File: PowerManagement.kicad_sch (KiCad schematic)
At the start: 27 parts, among them Q1 NMOS, U2 OKI-78SR-3.3_1.5-W36-C, U3 LM34966

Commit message: schematics done
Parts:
- removed C1: 100p, Capacitor_SMD:C_0603_1608Metric_Pad1.08x0.95mm_HandSolder, symbol Device:C
- removed C3: 10n, Capacitor_SMD:C_0603_1608Metric_Pad1.08x0.95mm_HandSolder, symbol Device:C
- removed C4, C6: 22n, Capacitor_SMD:C_0603_1608Metric_Pad1.08x0.95mm_HandSolder, symbol Device:C
- removed C5: 220p, Capacitor_SMD:C_0603_1608Metric_Pad1.08x0.95mm_HandSolder, symbol Device:C
- removed D1, D2: D, symbol Device:D
- removed L1: L, symbol Device:L
- removed Q1: NMOS, Package_TO_SOT_SMD:SOT-223-3_TabPin2, symbol Simulation_SPICE:NMOS
- removed R1, R2, R3: R, symbol Device:R
- removed R10: 11k3, Capacitor_SMD:C_0603_1608Metric_Pad1.08x0.95mm_HandSolder, symbol Device:R
- removed R11: 0, Resistor_SMD:R_0603_1608Metric_Pad0.98x0.95mm_HandSolder, symbol Device:R
- removed R12, R4: 10m, Resistor_SMD:R_0603_1608Metric_Pad0.98x0.95mm_HandSolder, symbol Device:R
- removed R5: 100, Resistor_SMD:R_0603_1608Metric_Pad0.98x0.95mm_HandSolder, symbol Device:R
- removed R7: 10k, Resistor_SMD:R_0603_1608Metric_Pad0.98x0.95mm_HandSolder, symbol Device:R
- removed R8: 6k8, Resistor_SMD:R_0603_1608Metric_Pad0.98x0.95mm_HandSolder, symbol Device:R
- removed R9: 49k9, Resistor_SMD:R_0603_1608Metric_Pad0.98x0.95mm_HandSolder, symbol Device:R
- removed U2: OKI-78SR-3.3_1.5-W36-C, Converter_DCDC:Converter_DCDC_Murata_OKI-78SR_Vertical, symbol Converter_DCDC:OKI-78SR-3.3_1.5-W36-C
- removed U3: LM34966, Package_SO:HTSSOP-14-1EP_4.4x5mm_P0.65mm_EP3.4x5mm_Mask3x3.1mm_ThermalVias, symbol 10_ICs:LM34966
- added C30, C33: 10n, Capacitor_SMD:C_0603_1608Metric_Pad1.08x0.95mm_HandSolder, symbol Device:C
- added C31, C32, C53: 1u, Capacitor_SMD:C_0805_2012Metric_Pad1.18x1.45mm_HandSolder, symbol Device:C
- added C54: 100n, Capacitor_SMD:C_0603_1608Metric_Pad1.08x0.95mm_HandSolder, symbol Device:C
- added C55: 1n, Capacitor_SMD:C_0603_1608Metric_Pad1.08x0.95mm_HandSolder, symbol Device:C
- added F1, F2, F3, F4: Polyfuse_Small, symbol Device:Polyfuse_Small
- added U12: OKI-78SR-3.3_1.5-W36H-C, Converter_DCDC:Converter_DCDC_Murata_OKI-78SR_Horizontal, symbol Converter_DCDC:OKI-78SR-3.3_1.5-W36H-C
- added U13: OKI-78SR-12_1.0-W36H-C, Converter_DCDC:Converter_DCDC_Murata_OKI-78SR_Horizontal, symbol Converter_DCDC:OKI-78SR-12_1.0-W36H-C
- added U14: MCP1501-30xSN, Package_SO:SOIC-8_3.9x4.9mm_P1.27mm, symbol Reference_Voltage:MCP1501-30xSN
- C2: value 1u -> 100n; footprint Capacitor_SMD:C_0805_2012Metric_Pad1.18x1.45mm_HandSolder -> Capacitor_SMD:C_0603_1608Metric_Pad1.08x0.95mm_HandSolder
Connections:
- net VCC is gone; now on net GND: C2.2
- net GND: now also C30.2, C31.1, C32.1, C33.2, C53.1, C54.2, C55.2, U12.2 (GND), U13.2 (GND), U14.2 (GND), U14.4 (GND), U14.5 (GND), U14.6 (GND); no longer C2.1
- net P3V3: now also C2.1, F3.2, U14.1 (VDD), U14.3 (~{SHDN}); no longer C26.2, C27.1
- net P24_6S_UNREGULATED renamed P15V-20V_5S_FUSED
- net P15V-20V_5S_FUSED: now also C30.1, C31.2, F2.2, U12.1 (IN), U13.1 (IN)
- new net: C26.2, C27.1, F3.1, U12.3 (OUT)
- new net: C32.2, C33.1, F4.1, U13.3 (OUT)
- new net P12V: F4.2
- new net P15V-20V_5S_UNREGULATED: F2.1
- new net P3V_REF: C53.2, C54.1, C55.1, U14.7 (OUT), U14.8 (FB)
- new net PHV: F1.2
- new net step-up/PHV: F1.1
- no-connect marks 1 -> 0
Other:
- added sheet step-up (step-up.kicad_sch)
- note added: "Recalculate values for step-up converter DONE find correct footprint and part inductor DONE add 3V reference DONE add POWER GOOD comparators hide step-up in separate hierarchical sheet DONE add PTC resistor(fuse) and schottky diodes DONE add wrong polarity and overvoltage on input protection"
- note removed: "Css = 22n for soft start aprox. 88us"
- note removed: "RT = 49k9 for switching frequency 440kHz"
- moved on the sheet: C26, C27, C28, C29

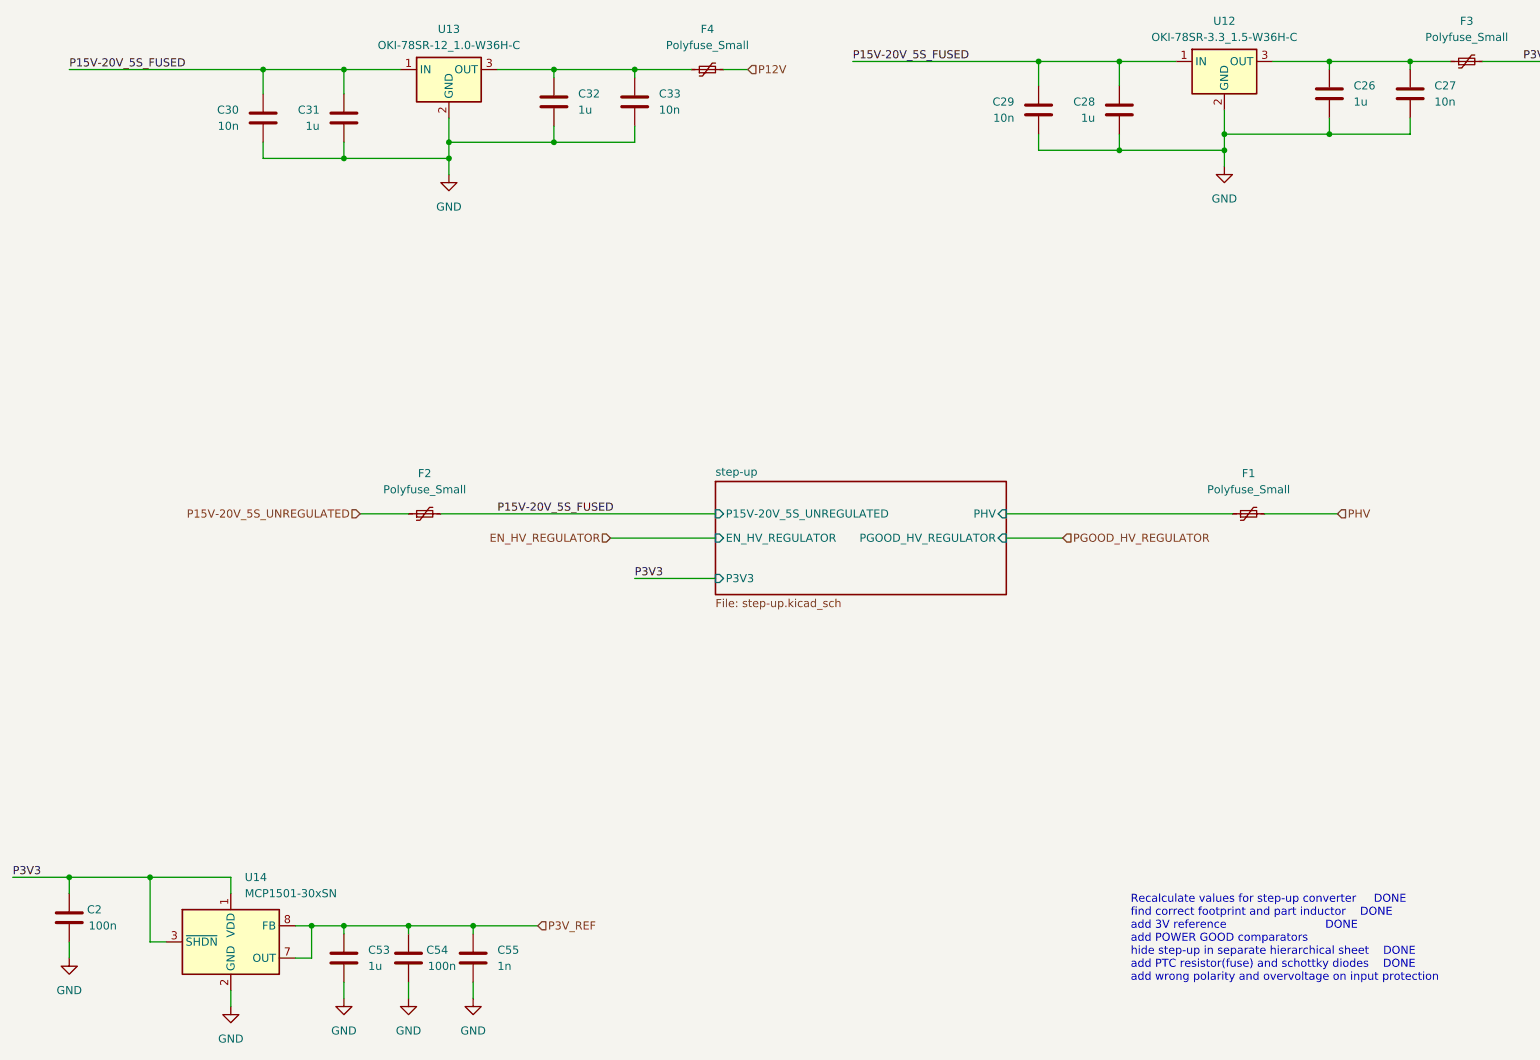
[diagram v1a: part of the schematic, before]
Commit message: ready schematic for layout
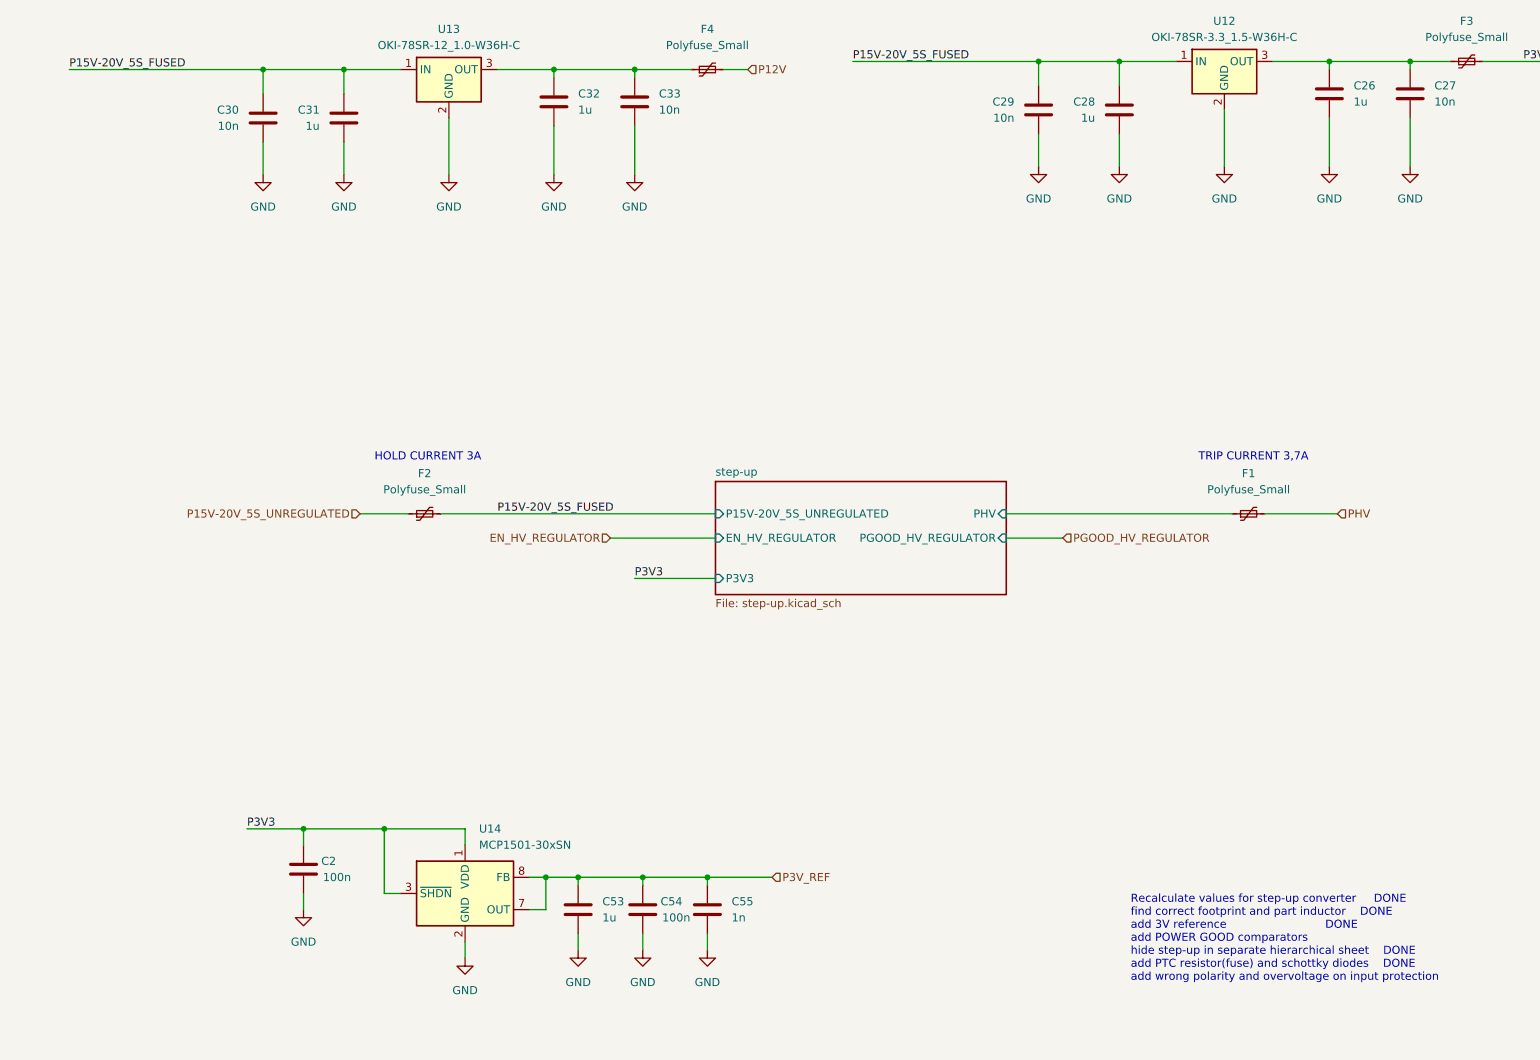
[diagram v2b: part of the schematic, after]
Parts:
- F1, F2: footprint (none) -> Fuse:Fuse_2920_7451Metric
- F3, F4: footprint (none) -> Fuse:Fuse_1206_3216Metric
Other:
- note added: "HOLD CURRENT 3A"
- note added: "TRIP CURRENT 3,7A"
- moved on the sheet: C2, C53, C54, C55, U14

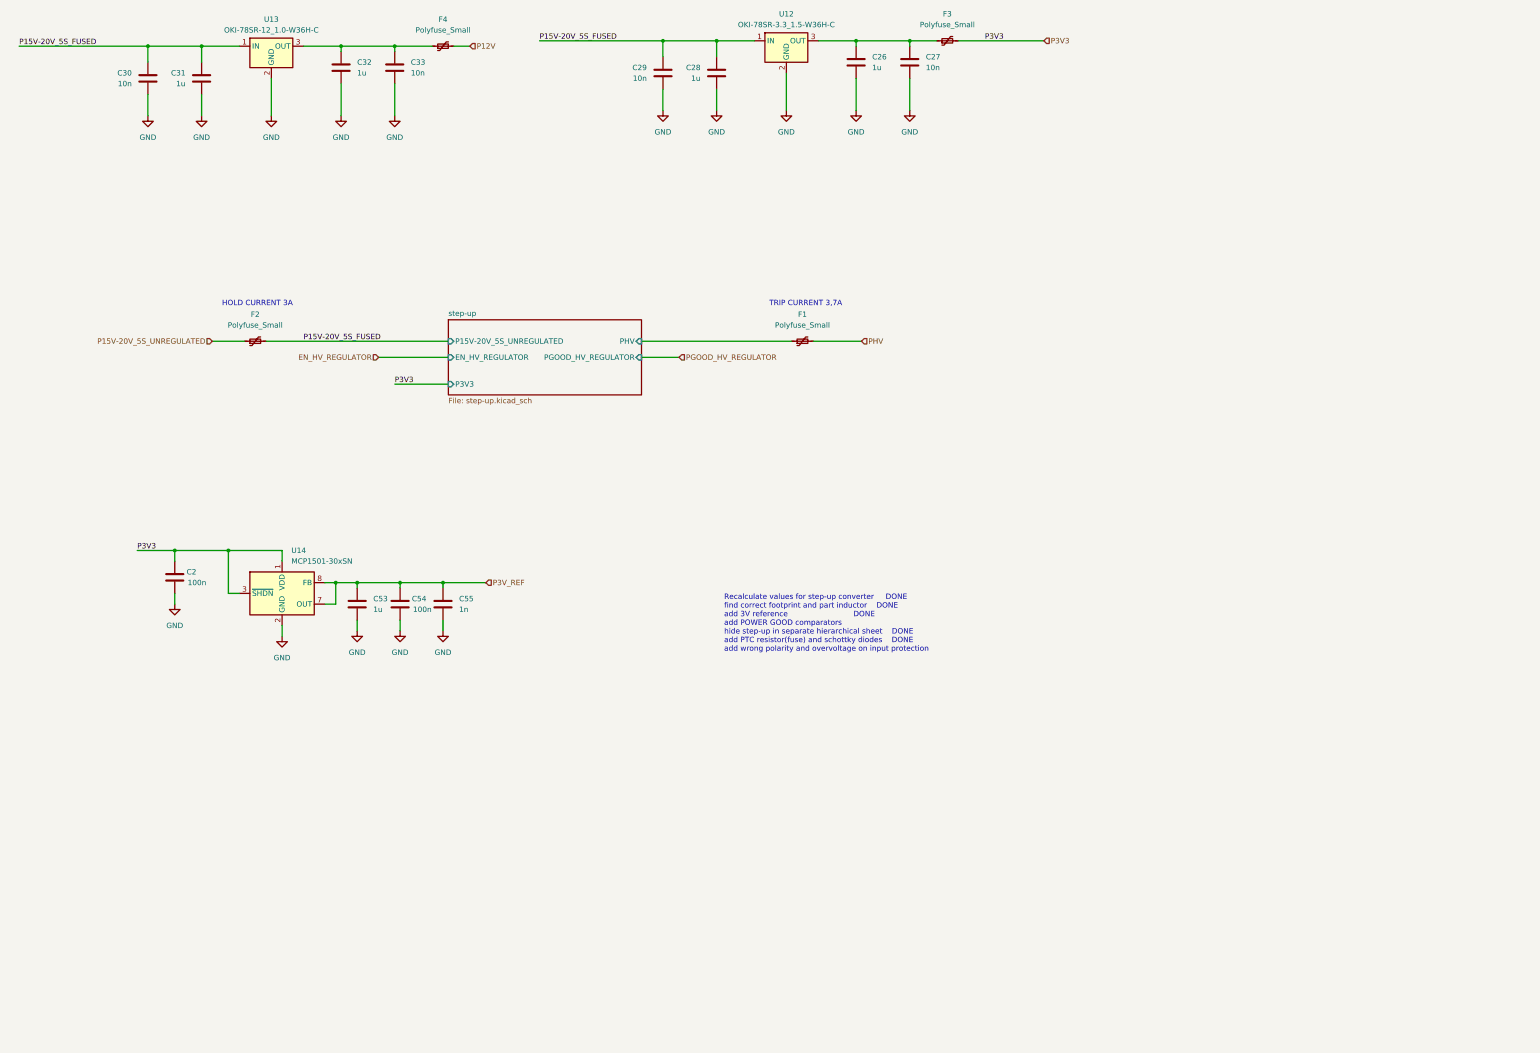
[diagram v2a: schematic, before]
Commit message: schematic ready, basic layout done
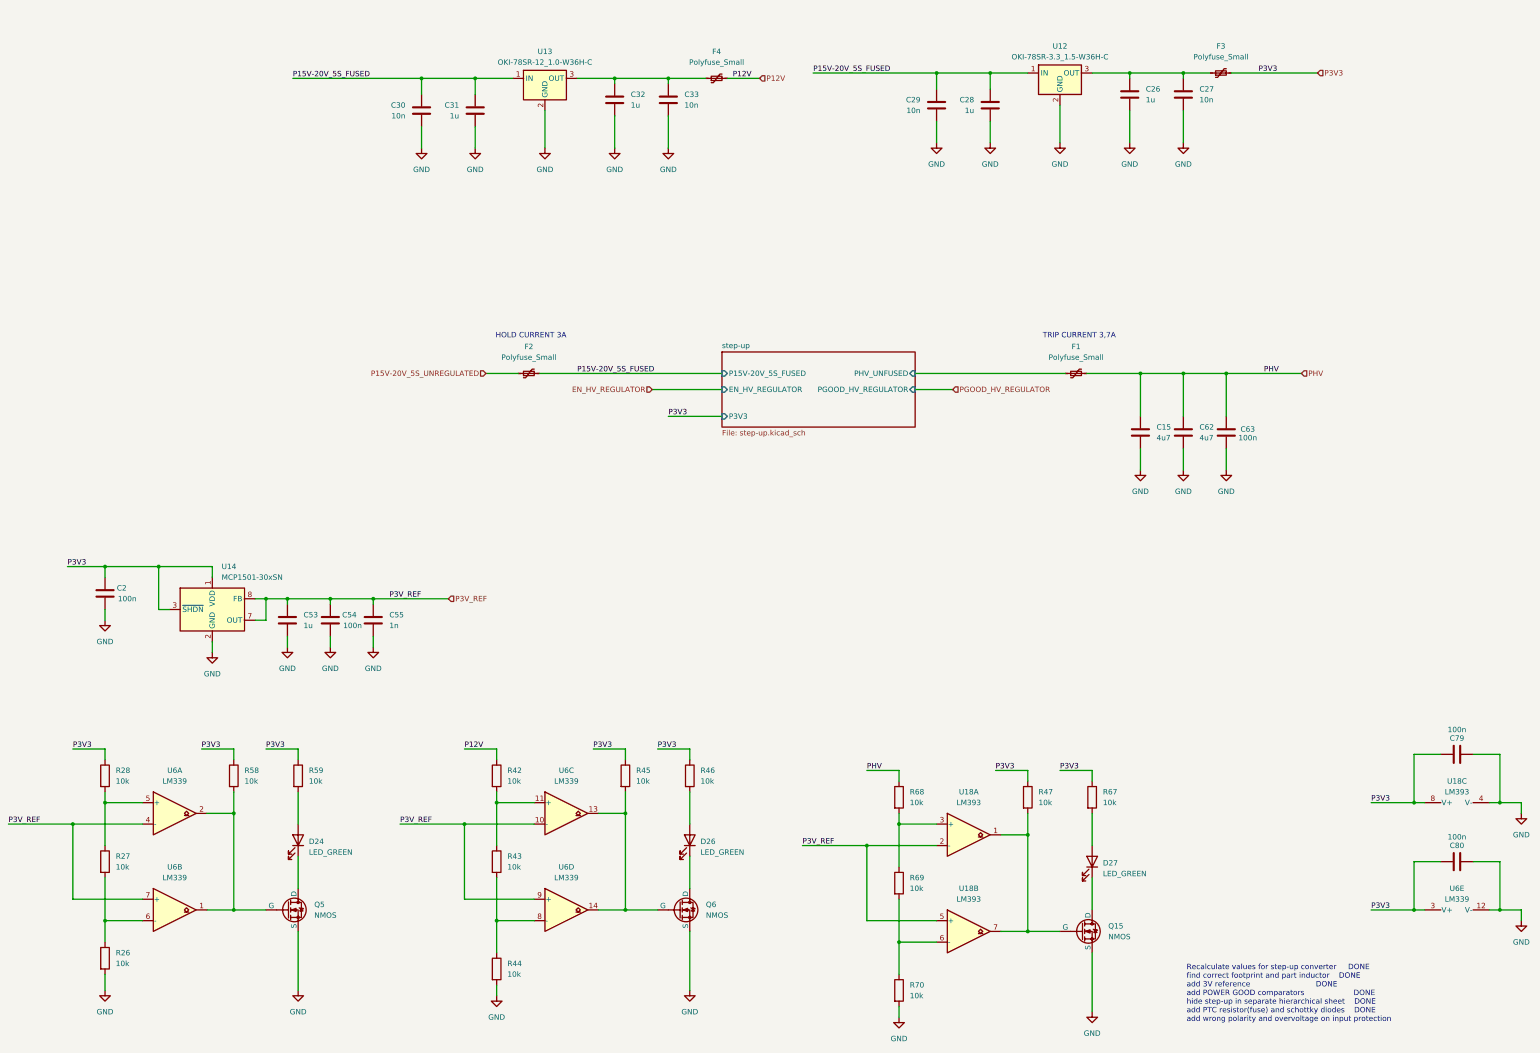
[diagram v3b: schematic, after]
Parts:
- added C15, C62: 4u7, Capacitor_SMD:C_0805_2012Metric_Pad1.18x1.45mm_HandSolder, symbol Device:C
- added C63, C79, C80: 100n, Capacitor_SMD:C_0603_1608Metric_Pad1.08x0.95mm_HandSolder, symbol Device:C
- added D24, D26, D27: LED_GREEN, LED_SMD:LED_0805_2012Metric_Pad1.15x1.40mm_HandSolder, symbol Device:LED
- added Q15, Q5, Q6: NMOS, Package_TO_SOT_SMD:SOT-23_Handsoldering, symbol Simulation_SPICE:NMOS
- added R26, R27, R28, R42, R43, R44, R45, R46, R47, R58, R59, R67, R68, R69, R70: 10k, Resistor_SMD:R_0603_1608Metric_Pad0.98x0.95mm_HandSolder, symbol Device:R
- added U18: LM393, Package_SO:TSSOP-8_4.4x3mm_P0.65mm, symbol Comparator:LM393
- added U6: LM339, Package_SO:TSSOP-14_4.4x5mm_P0.65mm, symbol Comparator:LM339
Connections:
- net GND: now also C15.1, C62.1, C63.2, C79.2, C80.2, Q15.3 (S), Q5.3 (S), Q6.3 (S), R26.2, R44.2, R70.2, U18.4 (V-), U6.12 (V-)
- net P12V: now also R42.1
- net P3V3: now also C79.1, C80.1, R28.1, R45.1, R46.1, R47.1, R58.1, R59.1, R67.1, U18.8 (V+), U6.3 (V+)
- net P3V_REF: now also U18.2 (-), U18.5 (+), U6.10 (-), U6.4 (-), U6.7 (+), U6.9 (+)
- net PHV: now also C15.2, C62.2, C63.1, R68.1
- net step-up/PHV renamed step-up/PHV_UNFUSED
- new net: D24.1 (K), Q5.1 (D)
- new net: D24.2 (A), R59.2
- new net: R26.1, R27.2, U6.6 (-)
- new net: R68.2, R69.1, U18.3 (+)
- new net: R69.2, R70.1, U18.6 (-)
- new net: D26.1 (K), Q6.1 (D)
- new net: D26.2 (A), R46.2
- new net: Q5.2 (G), R58.2, U6.1, U6.2
- new net: Q15.2 (G), R47.2, U18.1, U18.7
- new net: R27.1, R28.2, U6.5 (+)
- new net: R42.2, R43.1, U6.11 (+)
- new net: R43.2, R44.1, U6.8 (-)
- new net: Q6.2 (G), R45.2, U6.13, U6.14
- new net: D27.2 (A), R67.2
- new net: D27.1 (K), Q15.1 (D)
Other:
- sheet step-up ports: added P15V-20V_5S_FUSED, PHV_UNFUSED; removed P15V-20V_5S_UNREGULATED, PHV
- note added: "Recalculate values for step-up converter DONE find correct footprint and part inductor DONE add 3V reference DONE add POWER GOOD comparators DONE hide step-up in separate hierarchical sheet DONE add PTC resistor(fuse) and schottky diodes DONE add wrong polarity and overvoltage on input protection"
- note removed: "Recalculate values for step-up converter DONE find correct footprint and part inductor DONE add 3V reference DONE add POWER GOOD comparators hide step-up in separate hierarchical sheet DONE add PTC resistor(fuse) and schottky diodes DONE add wrong polarity and overvoltage on input protection"
- moved on the sheet: C2, C26, C27, C28, C29, C30, C31, C32, C33, C53, C54, C55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
